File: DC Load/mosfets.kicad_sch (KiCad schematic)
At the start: 66 parts, among them Q1 IRFP260, Q10 IRFP260, Q11 IRFP260, Q12 IRFP260, Q2 IRFP260, Q3 IRFP260, Q4 IRFP260, Q5 IRFP260, Q6 IRFP260, Q7 IRFP260, Q8 IRFP260, Q9 IRFP260, U1 OPA2182, U2 OPA2182, U3 OPA2182, U4 OPA2182, U5 OPA2182, U6 OPA2182

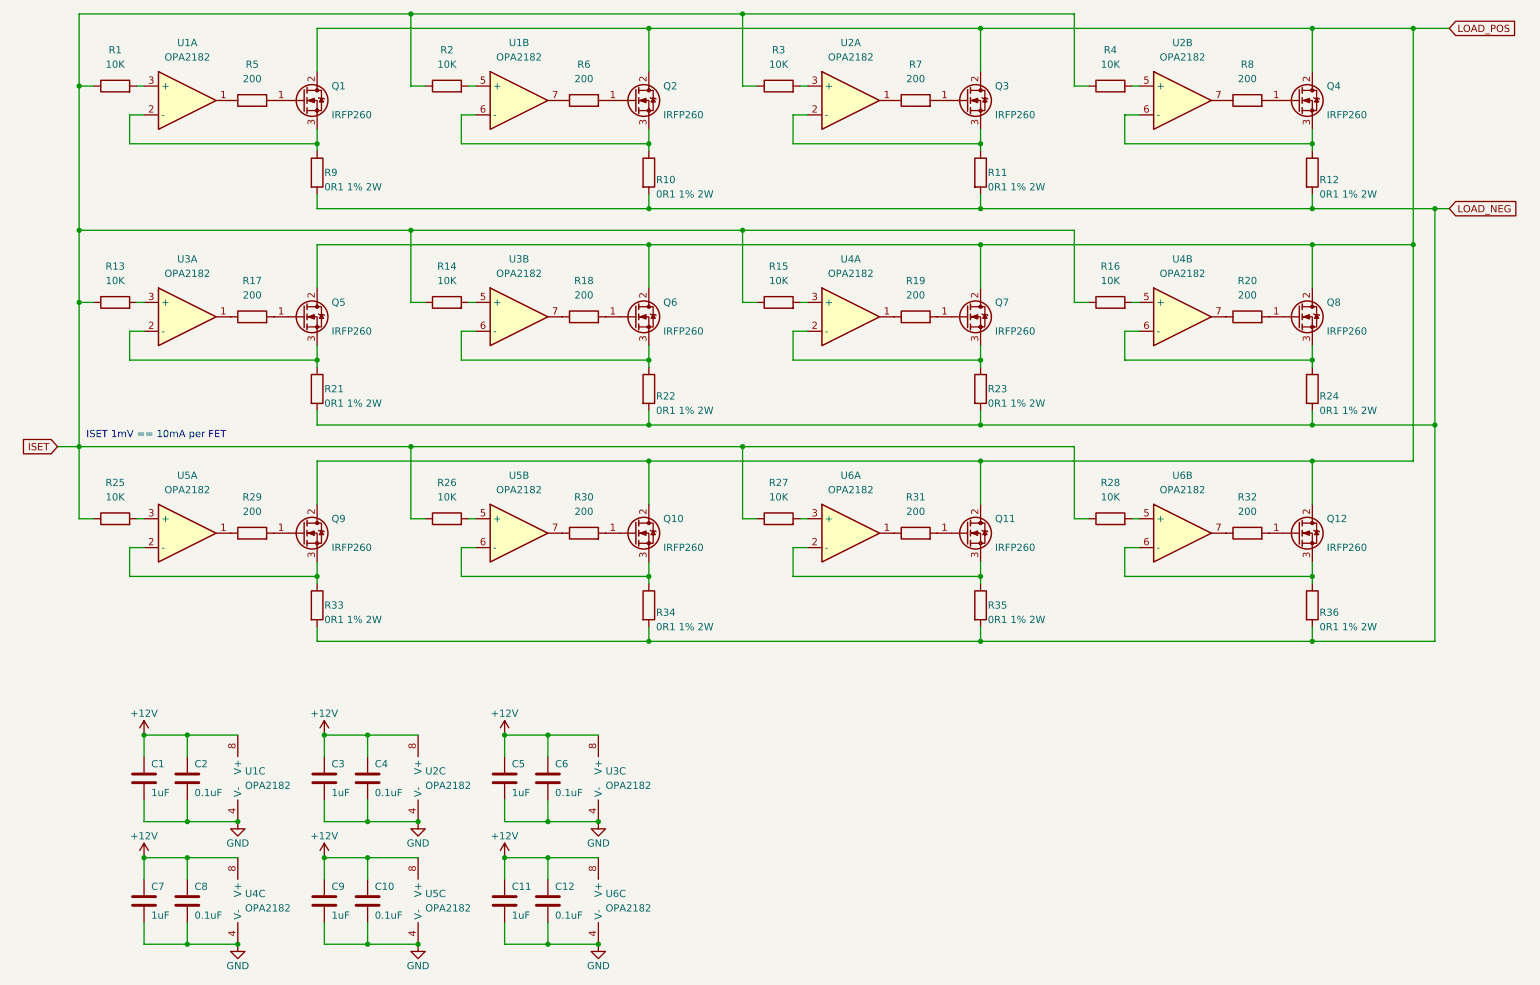
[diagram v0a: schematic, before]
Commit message: Use 8 load FETS instead of 12
Using 8 FETS makes output resolution easier to calculate when using a power of two volatage reference in the output DAC. Also cheaper and it's easier to fit fewer devices onto the heatsink area.
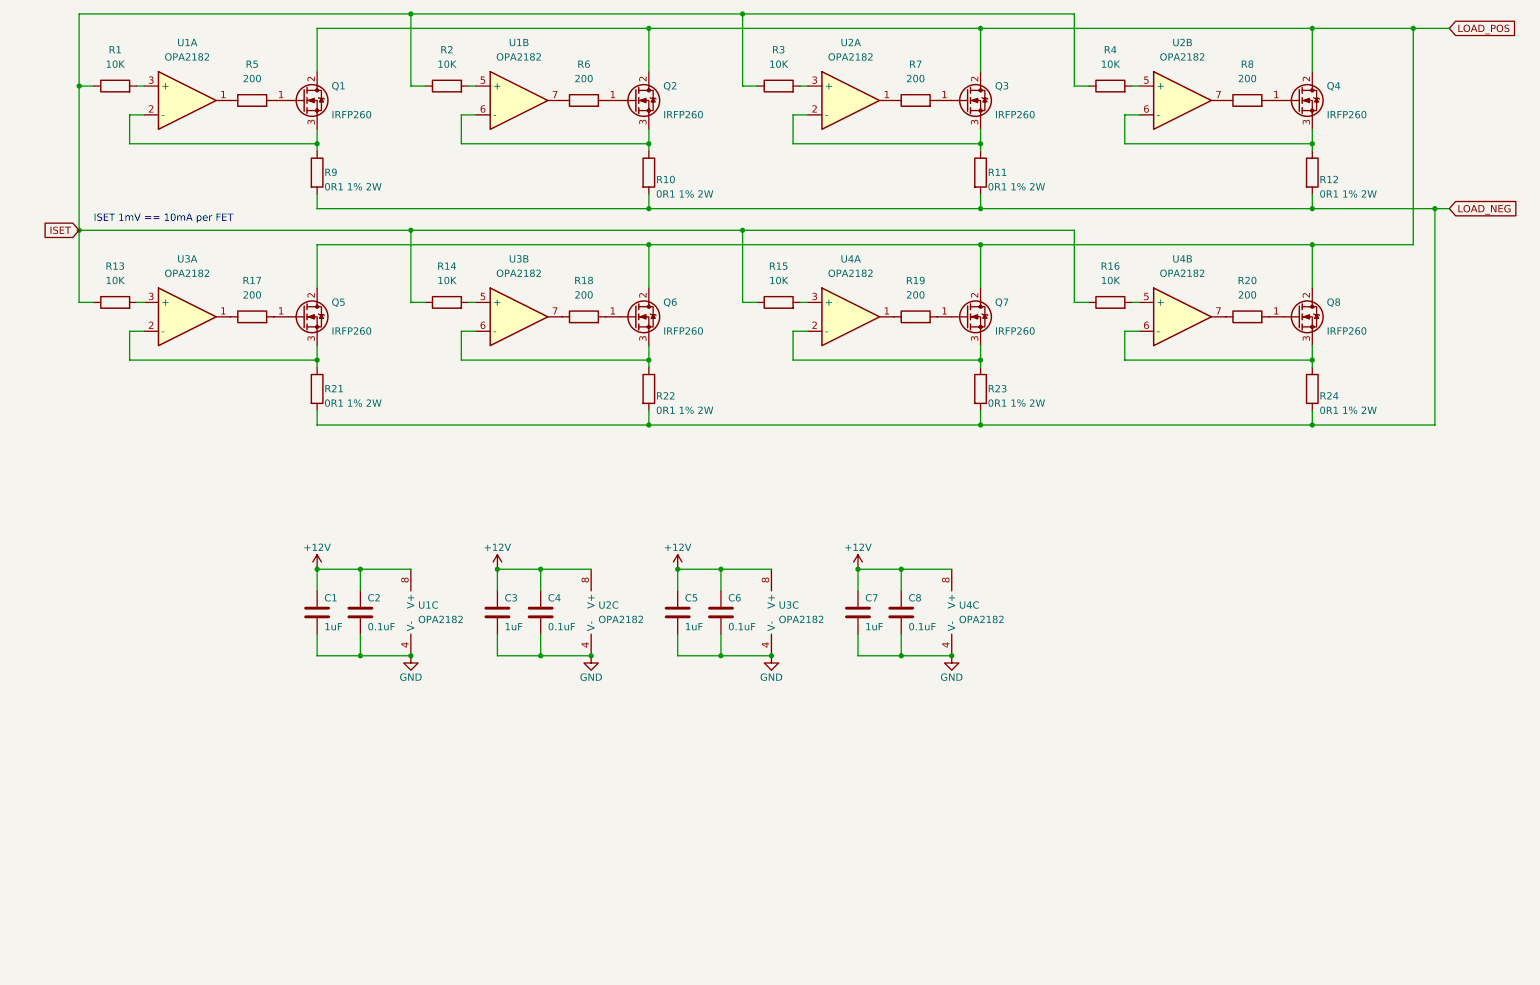
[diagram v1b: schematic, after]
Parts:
- removed C10, C12: 0.1uF, symbol Device:C
- removed C11, C9: 1uF, symbol Device:C
- removed Q10, Q11, Q12, Q9: IRFP260, Package_TO_SOT_THT:TO-247-3_Vertical, symbol Device:Q_NMOS_GDS
- removed R25, R26, R27, R28: 10K, symbol Device:R
- removed R29, R30, R31, R32: 200, symbol Device:R
- removed R33, R34, R35, R36: 0R1 1% 2W, symbol Device:R
- removed U5, U6: OPA2182, symbol Device:Opamp_Dual
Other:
- moved on the sheet: C1, C2, C3, C4, C5, C6, C7, C8, U1C, U2C, U3C, U4C

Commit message: Separate sheet for ADC and DAC
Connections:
- net LOAD_NEG renamed LOAD-
- net LOAD_POS renamed LOAD+
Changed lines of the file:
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@@
+    (stroke (width 0) (type default) (color 0 0 0 0))
+  )
+  (wire (pts (xy 22.86 59.69) (xy 25.4 59.69))
     (stroke (width 0) (type default) (color 0 0 0 0))
   )
@@
     (effects (font (size 1.27 1.27)) (justify left bottom))
   )
-  (global_label "LOAD_NEG" (shape input) (at 266.7 55.88 0) (fields_autoplaced)
+  (hierarchical_label "LOAD-" (shape output) (at 266.7 55.88 0)
     (effects (font (size 1.27 1.27)) (justify left))
-    (property "Intersheet References" "${INTERSHEET_REFS}" (id 0) (at 278.5474 55.8006 0)
-      (effects (font (size 1.27 1.27)) (justify left) hide)
-    )
-  )
-  (global_label "ISET" (shape input) (at 25.4 59.69 180) (fields_autoplaced)
+  )
+  (hierarchical_label "ISET" (shape input) (at 22.86 59.69 180)
     (effects (font (size 1.27 1.27)) (justify right))
-    (property "Intersheet References" "${INTERSHEET_REFS}" (id 0) (at 19.0559 59.6106 0)
-      (effects (font (size 1.27 1.27)) (justify right) hide)
-    )
-  )
-  (global_label "LOAD_POS" (shape input) (at 266.7 24.13 0) (fields_autoplaced)
+  )
+  (hierarchical_label "LOAD+" (shape input) (at 266.7 24.13 0)
     (effects (font (size 1.27 1.27)) (justify left))
-    (property "Intersheet References" "${INTERSHEET_REFS}" (id 0) (at 278.6079 24.0506 0)
-      (effects (font (size 1.27 1.27)) (justify left) hide)
-    )
   )
   (symbol (lib_id "Device:R") (at 242.57 87.63 0) (unit 1)

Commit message: Separate sheet for power supply
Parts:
- renumbered C1 to C?, C6 to C?, C3 to C?, C8 to C?, C7 to C?, C2 to C?, C5 to C?, C4 to C?, Q4 to Q?, Q5 to Q?, Q8 to Q?, Q2 to Q?, Q7 to Q?, Q1 to Q?, Q3 to Q?, Q6 to Q?, R24 to R?, R11 to R?, R6 to R?, R10 to R?, R13 to R?, R17 to R?, R12 to R?, R23 to R?, R19 to R?, R15 to R?, R20 to R?, R5 to R?, R22 to R?, R16 to R?, R4 to R?, R21 to R?, R2 to R?, R1 to R?, R7 to R?, R3 to R?, R9 to R?, R14 to R?, R8 to R?, R18 to R?, U3 to U?, U1 to U?, U2 to U?, U4 to U?

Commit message: update
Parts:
- gave numbers to parts that had none: 44

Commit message: Assign temporary footprints
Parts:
- C1, C2, C3, C4, C5, C6, C7, C8: footprint (none) -> Capacitor_SMD:C_0201_0603Metric
- R1, R13, R14, R15, R16, R17, R18, R19, R2, R20, R3, R4, R5, R6, R7, R8: footprint (none) -> Resistor_SMD:R_0603_1608Metric
- R10, R11, R12, R21, R22, R23, R24, R9: footprint (none) -> Resistor_THT:R_Axial_DIN0516_L15.5mm_D5.0mm_P20.32mm_Horizontal
- U1, U2, U4: footprint (none) -> Package_SO:VSSOP-8_3.0x3.0mm_P0.65mm

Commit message: Start board
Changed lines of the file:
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@@
   )
   (symbol (lib_id "Device:Q_NMOS_GDS") (at 240.03 36.83 0) (unit 1)
-    (in_bom yes) (on_board yes)
-    (property "Reference" "Q4" (id 0) (at 245.11 34.29 0)
-      (effects (font (size 1.27 1.27)) (justify left))
-    )
-    (property "Value" "IRFP260" (id 1) (at 245.11 39.37 0)
+    (in_bom yes) (on_board yes) (fields_autoplaced)
+    (property "Reference" "Q4" (id 0) (at 246.38 35.5599 0)
+      (effects (font (size 1.27 1.27)) (justify left))
+    )
+    (property "Value" "IRFP260" (id 1) (at 246.38 38.0999 0)
       (effects (font (size 1.27 1.27)) (justify left))
     )
@@
   )
   (symbol (lib_id "Device:Q_NMOS_GDS") (at 64.77 74.93 0) (unit 1)
-    (in_bom yes) (on_board yes)
-    (property "Reference" "Q5" (id 0) (at 69.85 72.39 0)
-      (effects (font (size 1.27 1.27)) (justify left))
-    )
-    (property "Value" "IRFP260" (id 1) (at 69.85 77.47 0)
+    (in_bom yes) (on_board yes) (fields_autoplaced)
+    (property "Reference" "Q5" (id 0) (at 71.12 73.6599 0)
+      (effects (font (size 1.27 1.27)) (justify left))
+    )
+    (property "Value" "IRFP260" (id 1) (at 71.12 76.1999 0)
       (effects (font (size 1.27 1.27)) (justify left))
     )
@@
   )
   (symbol (lib_id "Device:Q_NMOS_GDS") (at 240.03 74.93 0) (unit 1)
-    (in_bom yes) (on_board yes)
-    (property "Reference" "Q8" (id 0) (at 245.11 72.39 0)
-      (effects (font (size 1.27 1.27)) (justify left))
-    )
-    (property "Value" "IRFP260" (id 1) (at 245.11 77.47 0)
+    (in_bom yes) (on_board yes) (fields_autoplaced)
+    (property "Reference" "Q8" (id 0) (at 246.38 73.6599 0)
+      (effects (font (size 1.27 1.27)) (justify left))
+    )
+    (property "Value" "IRFP260" (id 1) (at 246.38 76.1999 0)
       (effects (font (size 1.27 1.27)) (justify left))
     )
@@
   )
   (symbol (lib_id "Device:Q_NMOS_GDS") (at 123.19 36.83 0) (unit 1)
-    (in_bom yes) (on_board yes)
-    (property "Reference" "Q2" (id 0) (at 128.27 34.29 0)
-      (effects (font (size 1.27 1.27)) (justify left))
-    )
-    (property "Value" "IRFP260" (id 1) (at 128.27 39.37 0)
+    (in_bom yes) (on_board yes) (fields_autoplaced)
+    (property "Reference" "Q2" (id 0) (at 129.54 35.5599 0)
+      (effects (font (size 1.27 1.27)) (justify left))
+    )
+    (property "Value" "IRFP260" (id 1) (at 129.54 38.0999 0)
       (effects (font (size 1.27 1.27)) (justify left))
     )
@@
   )
   (symbol (lib_id "Device:Q_NMOS_GDS") (at 181.61 74.93 0) (unit 1)
-    (in_bom yes) (on_board yes)
-    (property "Reference" "Q7" (id 0) (at 186.69 72.39 0)
-      (effects (font (size 1.27 1.27)) (justify left))
-    )
-    (property "Value" "IRFP260" (id 1) (at 186.69 77.47 0)
+    (in_bom yes) (on_board yes) (fields_autoplaced)
+    (property "Reference" "Q7" (id 0) (at 187.96 73.6599 0)
+      (effects (font (size 1.27 1.27)) (justify left))
+    )
+    (property "Value" "IRFP260" (id 1) (at 187.96 76.1999 0)
       (effects (font (size 1.27 1.27)) (justify left))
     )
@@
   )
   (symbol (lib_id "Device:Q_NMOS_GDS") (at 64.77 36.83 0) (unit 1)
-    (in_bom yes) (on_board yes)
-    (property "Reference" "Q1" (id 0) (at 69.85 34.29 0)
-      (effects (font (size 1.27 1.27)) (justify left))
-    )
-    (property "Value" "IRFP260" (id 1) (at 69.85 39.37 0)
+    (in_bom yes) (on_board yes) (fields_autoplaced)
+    (property "Reference" "Q1" (id 0) (at 71.12 35.5599 0)
+      (effects (font (size 1.27 1.27)) (justify left))
+    )
+    (property "Value" "IRFP260" (id 1) (at 71.12 38.0999 0)
       (effects (font (size 1.27 1.27)) (justify left))
     )
@@
       (effects (font (size 1.27 1.27)) hide)
     )
-    (property "Datasheet" "~" (id 3) (at 64.77 36.83 0)
+    (property "Datasheet" "https://au.mouser.com/datasheet/2/196/Infineon_IRFP260N_DataSheet_v01_01_EN-1228493.pdf" (id 3) (at 64.77 36.83 0)
       (effects (font (size 1.27 1.27)) hide)
     )
@@
   )
   (symbol (lib_id "Device:Q_NMOS_GDS") (at 181.61 36.83 0) (unit 1)
-    (in_bom yes) (on_board yes)
-    (property "Reference" "Q3" (id 0) (at 186.69 34.29 0)
-      (effects (font (size 1.27 1.27)) (justify left))
-    )
-    (property "Value" "IRFP260" (id 1) (at 186.69 39.37 0)
+    (in_bom yes) (on_board yes) (fields_autoplaced)
+    (property "Reference" "Q3" (id 0) (at 187.96 35.5599 0)
+      (effects (font (size 1.27 1.27)) (justify left))
+    )
+    (property "Value" "IRFP260" (id 1) (at 187.96 38.0999 0)
       (effects (font (size 1.27 1.27)) (justify left))
     )
@@
   )
   (symbol (lib_id "Device:Q_NMOS_GDS") (at 123.19 74.93 0) (unit 1)
-    (in_bom yes) (on_board yes)
-    (property "Reference" "Q6" (id 0) (at 128.27 72.39 0)
-      (effects (font (size 1.27 1.27)) (justify left))
-    )
-    (property "Value" "IRFP260" (id 1) (at 128.27 77.47 0)
-      (effects (font (size 1.27 1.27)) (justify left))
-    )
+    (in_bom yes) (on_board yes) (fields_autoplaced)
+    (property "Reference" "Q6" (id 0) (at 129.54 73.6599 0)
+      (effects (font (size 1.27 1.27)) (justify left))
+    )
+    (property "Value" "IRFP260" (id 1) (at 129.54 76.1999 0)
+      (effects (font (size 1.27 1.27)) (justify left))
+    )
